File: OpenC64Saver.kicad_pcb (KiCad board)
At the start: 2 copper layers, 33.3 x 43.2 mm, 16 parts, among them J1 Power I/O, Q1 PN2222A, Q2 PN2222A

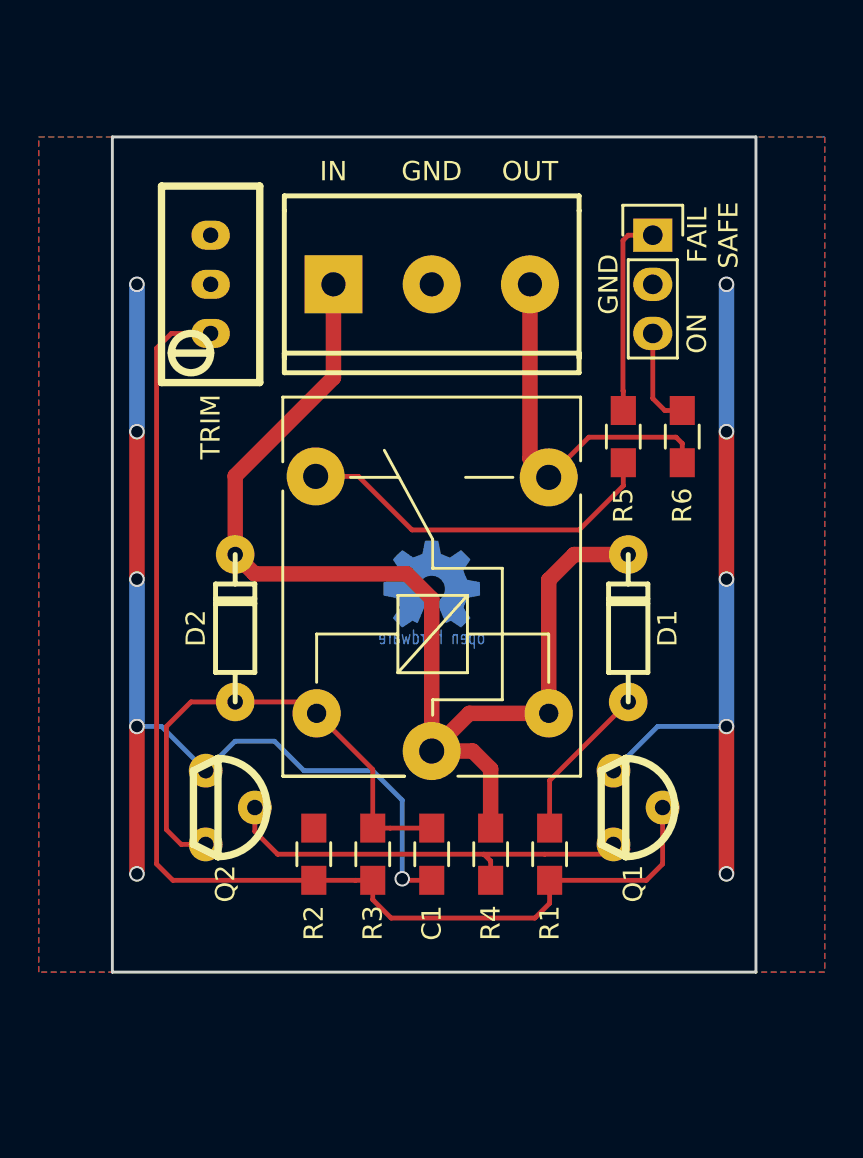
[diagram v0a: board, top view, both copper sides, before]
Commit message: Full board redesign to make it narrower
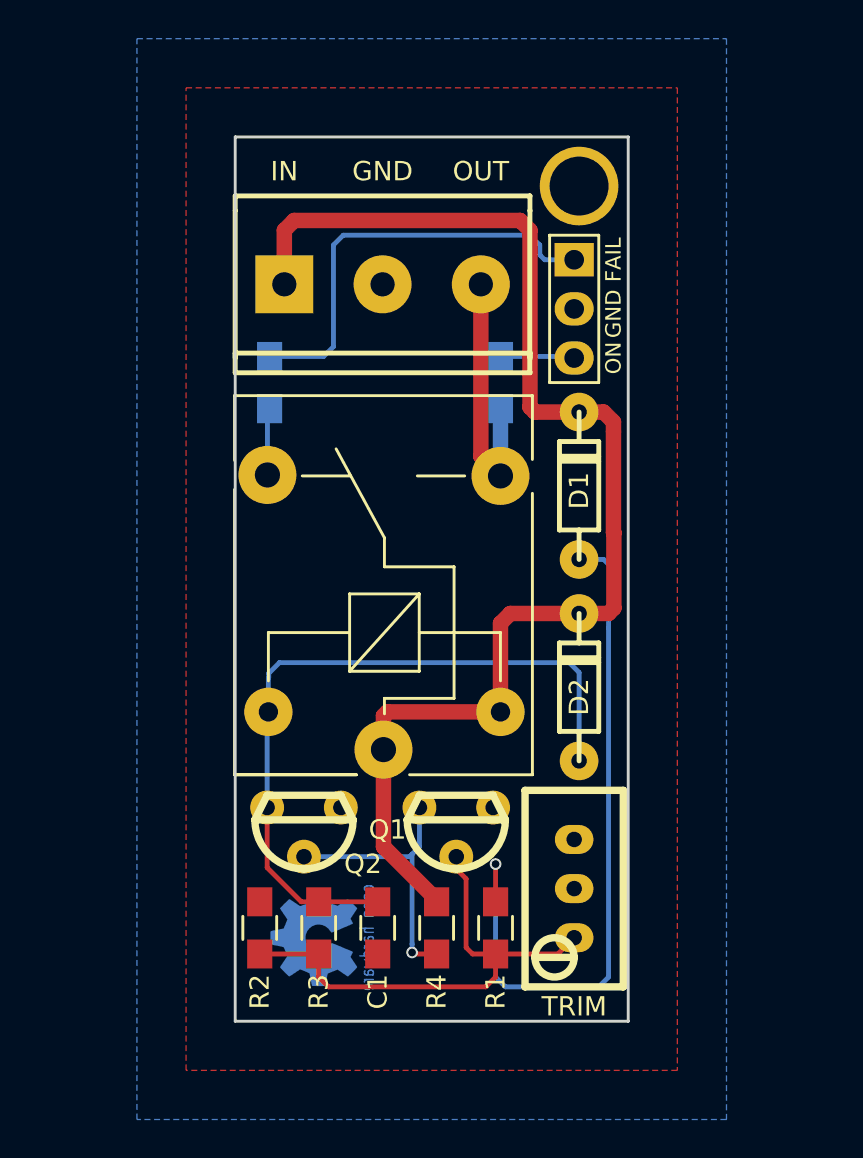
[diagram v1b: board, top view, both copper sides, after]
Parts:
- added REF**: 1pin, Connectors:1pin, F.Cu at (154.9, 76.2)
- R5, R6: moved to B.Cu
- moved R7 36.5 mm to (154.7, 112.5)
- moved G*** 19.3 mm to (141.2, 115.1), turned to 270 degrees
- moved R5 18.5 mm to (138.9, 86.4)
- moved D2 18.0 mm to (154.9, 102.1)
- moved R6 9.80 mm to (150.9, 86.4)
- moved Q1 8.79 mm to (148.6, 109.0), turned to 180 degrees
- moved D1 7.79 mm to (154.9, 91.7)
- moved C1 4.72 mm to (144.5, 114.6)
- moved R1 4.72 mm to (150.6, 114.6)
- moved R2 4.72 mm to (138.4, 114.6)
- moved R3 4.72 mm to (141.5, 114.6)
- moved R4 4.72 mm to (147.6, 114.6)
- moved Q2 4.49 mm to (140.7, 109.0), turned to 180 degrees
- moved D3 4.26 mm to (154.7, 80.0)
- moved J1 2.54 mm to (144.8, 81.3)
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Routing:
- net GND: track 89.9 -> 0.00 mm, vias 11 -> 0
- net Net-(Q1-Pad2): track 62.5 -> 26.0 mm
- net Net-(D1-Pad2): track 8.21 -> 37.0 mm, vias 0 -> 1
- net Net-(R6-Pad1): track 19.2 -> 3.47 mm
- net Net-(D3-Pad1): track 10.5 -> 22.2 mm
- net Net-(C1-Pad1): track 26.4 -> 37.6 mm
- net Net-(Q1-Pad3): track 22.3 -> 14.6 mm, vias 0 -> 1
- net VCC: track 60.0 -> 67.0 mm
- net +5V: track 19.3 -> 13.8 mm
- net Net-(D3-Pad3): track 5.14 -> 3.84 mm
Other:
- board size 33.3 x 43.2 mm -> 20.3 x 45.7 mm
- board text added: "FAIL"
- board text added: "V2"
- board text removed: "FAIL SAFE"
- board text removed: "V1.5"

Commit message: Make board slightly larger so silkscreen doesn't get cut
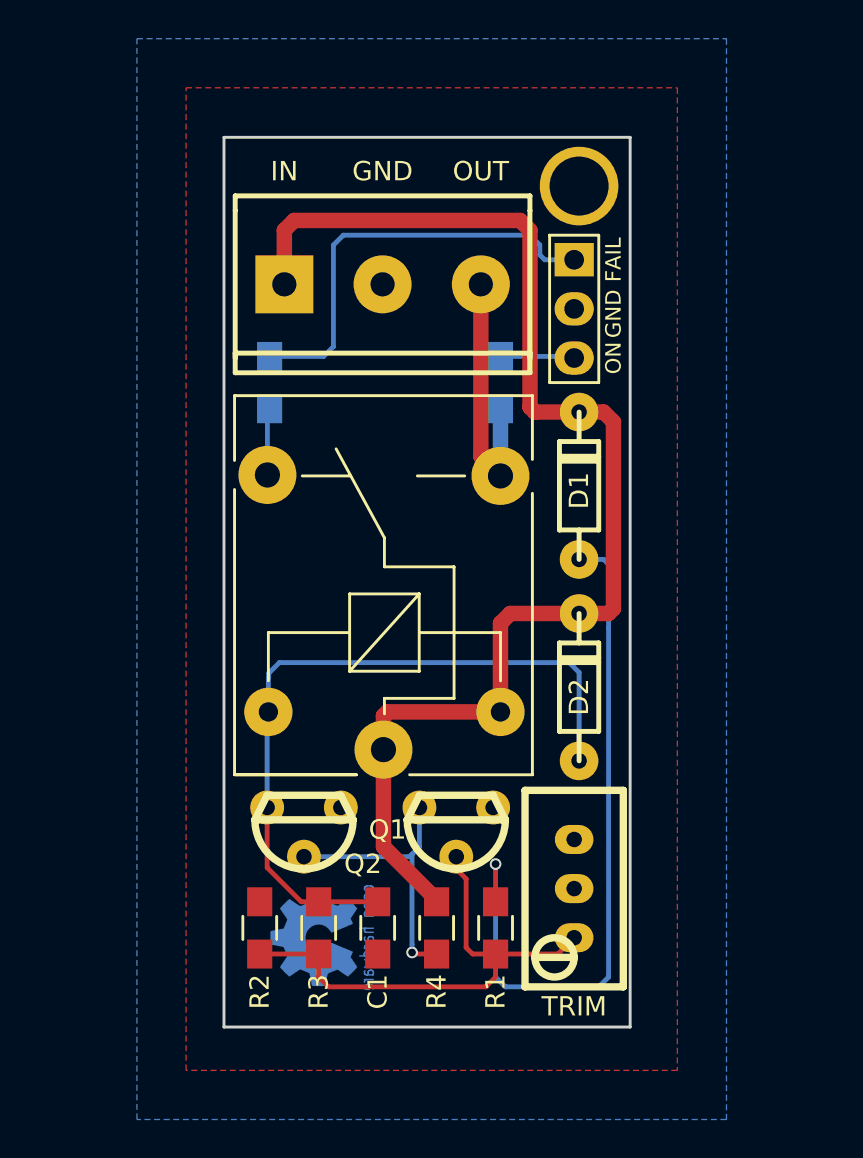
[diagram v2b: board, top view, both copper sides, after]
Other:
- board size 20.3 x 45.7 mm -> 21 x 46 mm
- net class Power: clearance 0.4 -> 0.2
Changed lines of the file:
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@@
-(kicad_pcb (version 4) (host pcbnew 4.0.6)
+(kicad_pcb (version 4) (host pcbnew 4.0.7)
   (general
     (links 27)
     (no_connects 0)
-    (area 137.084999 73.584999 157.555001 119.455001)
+    (area 136.504999 73.604999 157.655001 119.755001)
     (thickness 1.6)
     (drawings 15)
-    (tracks 87)
+    (tracks 84)
     (zones 0)
     (modules 17)
@@
     (pad_to_mask_clearance 0.2)
     (aux_axis_origin 0 0)
+    (grid_origin 157.58 119.68)
     (visible_elements FFFFFF7F)
     (pcbplotparams
@@
   )
   (net_class Power ""
-    (clearance 0.4)
+    (clearance 0.2)
     (trace_width 0.8)
     (via_dia 0.8)
@@
       (xy -1.51384 -2.24536)) (layer B.Cu) (width 0.00254))
   )
-  (dimension 20.32 (width 0.3) (layer F.Fab)
-    (gr_text "20,320 mm" (at 147.32 128.35) (layer F.Fab)
+  (dimension 21 (width 0.3) (layer F.Fab)
+    (gr_text "21.000 mm" (at 147.08 128.65) (layer F.Fab)
       (effects (font (size 1.5 1.5) (thickness 0.3)))
     )
-    (feature1 (pts (xy 137.16 119.38) (xy 137.16 129.7)))
-    (feature2 (pts (xy 157.48 119.38) (xy 157.48 129.7)))
-    (crossbar (pts (xy 157.48 127) (xy 137.16 127)))
-    (arrow1a (pts (xy 137.16 127) (xy 138.286504 126.413579)))
-    (arrow1b (pts (xy 137.16 127) (xy 138.286504 127.586421)))
-    (arrow2a (pts (xy 157.48 127) (xy 156.353496 126.413579)))
-    (arrow2b (pts (xy 157.48 127) (xy 156.353496 127.586421)))
-  )
-  (dimension 45.72 (width 0.3) (layer F.Fab)
-    (gr_text "45,720 mm" (at 166.45 96.52 270) (layer F.Fab)
+    (feature1 (pts (xy 136.58 119.68) (xy 136.58 130)))
+    (feature2 (pts (xy 157.58 119.68) (xy 157.58 130)))
+    (crossbar (pts (xy 157.58 127.3) (xy 136.58 127.3)))
+    (arrow1a (pts (xy 136.58 127.3) (xy 137.706504 126.713579)))
+    (arrow1b (pts (xy 136.58 127.3) (xy 137.706504 127.886421)))
+    (arrow2a (pts (xy 157.58 127.3) (xy 156.453496 126.713579)))
+    (arrow2b (pts (xy 157.58 127.3) (xy 156.453496 127.886421)))
+  )
+  (dimension 46 (width 0.3) (layer F.Fab)
+    (gr_text "46.000 mm" (at 166.55 96.68 270) (layer F.Fab)
       (effects (font (size 1.5 1.5) (thickness 0.3)))
     )
-    (feature1 (pts (xy 157.48 119.38) (xy 167.8 119.38)))
-    (feature2 (pts (xy 157.48 73.66) (xy 167.8 73.66)))
-    (crossbar (pts (xy 165.1 73.66) (xy 165.1 119.38)))
-    (arrow1a (pts (xy 165.1 119.38) (xy 164.513579 118.253496)))
-    (arrow1b (pts (xy 165.1 119.38) (xy 165.686421 118.253496)))
-    (arrow2a (pts (xy 165.1 73.66) (xy 164.513579 74.786504)))
-    (arrow2b (pts (xy 165.1 73.66) (xy 165.686421 74.786504)))
-  )
-  (gr_line (start 137.16 119.38) (end 137.16 73.66) (layer Edge.Cuts) (width 0.15))
-  (gr_line (start 157.48 119.38) (end 137.16 119.38) (layer Edge.Cuts) (width 0.15))
-  (gr_line (start 157.48 73.66) (end 157.48 119.38) (layer Edge.Cuts) (width 0.15))
-  (gr_line (start 137.16 73.66) (end 157.48 73.66) (layer Edge.Cuts) (width 0.15))
+    (feature1 (pts (xy 157.58 119.68) (xy 167.9 119.68)))
+    (feature2 (pts (xy 157.58 73.68) (xy 167.9 73.68)))
+    (crossbar (pts (xy 165.2 73.68) (xy 165.2 119.68)))
+    (arrow1a (pts (xy 165.2 119.68) (xy 164.613579 118.553496)))
+    (arrow1b (pts (xy 165.2 119.68) (xy 165.786421 118.553496)))
+    (arrow2a (pts (xy 165.2 73.68) (xy 164.613579 74.806504)))
+    (arrow2b (pts (xy 165.2 73.68) (xy 165.786421 74.806504)))
+  )
+  (gr_line (start 136.58 119.68) (end 136.58 73.68) (layer Edge.Cuts) (width 0.15))
+  (gr_line (start 157.58 119.68) (end 136.58 119.68) (layer Edge.Cuts) (width 0.15))
+  (gr_line (start 157.58 73.68) (end 157.58 119.68) (layer Edge.Cuts) (width 0.15))
+  (gr_line (start 136.58 73.68) (end 157.58 73.68) (layer Edge.Cuts) (width 0.15))
   (gr_text V2 (at 156.464 118.11 90) (layer B.SilkS)
     (effects (font (size 1 0.9) (thickness 0.15)) (justify mirror))
@@
     (effects (font (size 0.8 0.8) (thickness 0.15)))
   )
-  (gr_text TRIM (at 154.686 118.618 360) (layer F.SilkS)
+  (gr_text TRIM (at 154.686 118.618) (layer F.SilkS)
     (effects (font (size 1 1) (thickness 0.15)))
   )
@@
   (segment (start 138.811 108.331) (end 138.811 103.451) (width 0.25) (layer B.Cu) (net 1))
   (segment (start 138.811 103.451) (end 138.876 103.386) (width 0.25) (layer B.Cu) (net 1))
-  (segment (start 156.21 87.884) (end 154.94 87.884) (width 0.8) (layer F.Cu) (net 3))
-  (segment (start 156.718 88.392) (end 156.21 87.884) (width 0.8) (layer F.Cu) (net 3))
-  (segment (start 156.718 88.9) (end 156.718 94.110752) (width 0.8) (layer F.Cu) (net 3))
-  (segment (start 156.718 88.9) (end 156.718 88.392) (width 0.8) (layer F.Cu) (net 3))
+  (segment (start 154.94 87.884) (end 156.21 87.884) (width 0.8) (layer F.Cu) (net 3))
+  (segment (start 156.21 87.884) (end 156.718 88.392) (width 0.8) (layer F.Cu) (net 3))
+  (segment (start 156.718 88.392) (end 156.718 98.044) (width 0.8) (layer F.Cu) (net 3))
+  (segment (start 156.718 98.044) (end 156.464 98.298) (width 0.8) (layer F.Cu) (net 3))
+  (segment (start 156.464 98.298) (end 154.94 98.298) (width 0.8) (layer F.Cu) (net 3))
   (segment (start 139.7 81.28) (end 139.7 78.486) (width 0.8) (layer F.Cu) (net 3))
   (segment (start 139.7 78.486) (end 140.208 77.978) (width 0.8) (layer F.Cu) (net 3))
@@
   (segment (start 147.574 113.104) (end 147.574 113.204) (width 0.8) (layer F.Cu) (net 3))
   (segment (start 144.826 110.356) (end 147.574 113.104) (width 0.8) (layer F.Cu) (net 3))
-  (segment (start 156.739491 98.022509) (end 156.464 98.298) (width 0.8) (layer F.Cu) (net 3))
-  (segment (start 156.464 98.298) (end 154.94 98.298) (width 0.8) (layer F.Cu) (net 3))
-  (segment (start 156.718 94.110752) (end 156.739491 94.132243) (width 0.8) (layer F.Cu) (net 3))
-  (segment (start 156.739491 94.132243) (end 156.739491 98.022509) (width 0.8) (layer F.Cu) (net 3))
   (segment (start 144.826 103.586) (end 145.026 103.386) (width 0.8) (layer F.Cu) (net 3))
   (segment (start 145.026 103.386) (end 150.876 103.386) (width 0.8) (layer F.Cu) (net 3))

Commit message: Tighter soldermask
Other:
- rule pad_to_mask_clearance: 0.2 -> 0
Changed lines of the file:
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@@
     (pad_size 4.064 4.064)
     (pad_drill 3.048)
-    (pad_to_mask_clearance 0.2)
+    (pad_to_mask_clearance 0)
     (aux_axis_origin 0 0)
     (grid_origin 157.58 119.68)
@@
     (connect_pads (clearance 0.1524))
     (min_thickness 0.0254)
-    (fill yes (arc_segments 16) (thermal_gap 0.508) (thermal_bridge_width 0.508))
+    (fill yes (arc_segments 16) (thermal_gap 0.254) (thermal_bridge_width 0.508))
     (polygon
       (pts
@@
     (connect_pads (clearance 0.1524))
     (min_thickness 0.0254)
-    (fill yes (arc_segments 16) (thermal_gap 0.508) (thermal_bridge_width 0.508))
+    (fill yes (arc_segments 16) (thermal_gap 0.254) (thermal_bridge_width 0.508))
     (polygon
       (pts

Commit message: Bump version
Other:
- board text added: "V3"
- board text removed: "V2"
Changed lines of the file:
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@@
     (39 F.Mask user)
     (44 Edge.Cuts user)
-    (49 F.Fab user)
+    (49 F.Fab user hide)
   )
   (setup
@@
   (gr_line (start 157.58 73.68) (end 157.58 119.68) (layer Edge.Cuts) (width 0.15))
   (gr_line (start 136.58 73.68) (end 157.58 73.68) (layer Edge.Cuts) (width 0.15))
-  (gr_text V2 (at 156.464 118.11 90) (layer B.SilkS)
-    (effects (font (size 1 0.9) (thickness 0.15)) (justify mirror))
+  (gr_text V3 (at 156.464 118.11 90) (layer B.SilkS)
+    (effects (font (size 1 1) (thickness 0.15)) (justify mirror))
   )
   (gr_text github.com/SukkoPera/OpenC64Saver (at 147.32 94.488 90) (layer B.SilkS)
